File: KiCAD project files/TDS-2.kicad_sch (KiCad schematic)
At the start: 22 parts, among them J1 Barrel_Jack_MountingPin, J2 Conn_01x03_Pin, J3 Conn_01x03_Pin, J4 Conn_01x03_Pin, J5 SN49B14B, J6 SN49B14B, U1 TL072

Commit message: Added schematic and PCB design
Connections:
- net GNDREF: now also J5.R, J6.R
- net in: now also J5.T
- net out: no longer J6.R
- net at C2.1, J3.1 (Pin_1): no longer J5.R, J5.T
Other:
- note added: "Buffer"
- note added: "distortion"
- note added: "non-inverting amp"
- note added: "volume"
- moved on the sheet: J6

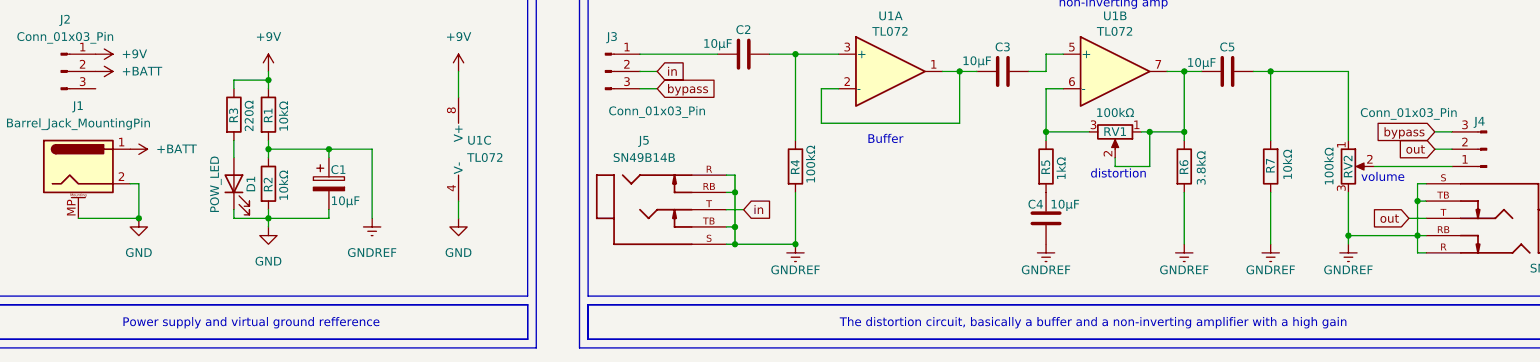
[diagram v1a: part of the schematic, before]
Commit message: Changed the ground values
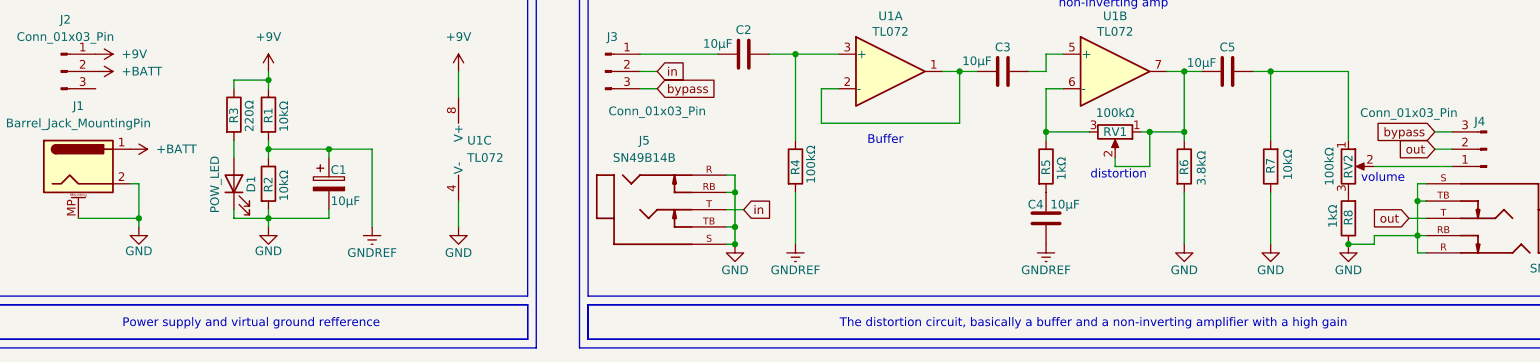
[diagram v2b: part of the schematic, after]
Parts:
- added R8: 1kΩ, Resistor_THT:R_Axial_DIN0207_L6.3mm_D2.5mm_P10.16mm_Horizontal, symbol Device:R
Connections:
- net GND: now also J5.R, J5.RB, J5.S, J5.TB, J6.R, J6.RB, J6.S, J6.TB, R6.2, R7.1, R8.1
- net GNDREF: no longer J5.R, J5.RB, J5.S, J5.TB, J6.R, J6.RB, J6.S, J6.TB, R6.2, R7.1, RV2.3
- new net: R8.2, RV2.3

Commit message: Update
Updated the schematic, idk about the photos tho
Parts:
- removed J2, J3, J4: Conn_01x03_Pin, Connector_PinHeader_2.54mm:PinHeader_1x03_P2.54mm_Vertical, symbol Connector:Conn_01x03_Pin
- added D2, D3: 1N4007, Diode_THT:D_DO-41_SOD81_P10.16mm_Horizontal, symbol Diode:1N4007
- added FTSW1: ~, Library:3PDT Footswitch, symbol footswitch:3PDT_Footswitch
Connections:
- net +9V: now also FTSW1.2
- net +BATT: now also FTSW1.1
- net GND: no longer J5.R, J5.RB, J5.S, J5.TB, J6.R, J6.RB, J6.S, J6.TB, R6.2, R7.1, R8.1
- net GNDREF: now also J5.R, J5.RB, J5.S, J5.TB, J6.R, J6.RB, J6.S, J6.TB, R6.2, R7.1, R8.1, D2.1 (K), D3.2 (A)
- net bypass: now also FTSW1.6, FTSW1.9
- net in: now also FTSW1.4
- net out: now also FTSW1.7
- net dst in: now reaches C2.1
- net dst in: now also FTSW1.5
- net at C5.2, R7.2, RV2.1: now also D2.2 (A), D3.1 (K)
- net dst out: now reaches RV2.2
- net dst out: now also FTSW1.8
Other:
- moved on the sheet: C1, C2, C3, C4, C5, D1, J1, J5, J6, R1, R2, R3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
